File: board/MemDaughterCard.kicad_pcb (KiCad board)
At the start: 2 copper layers, 87 x 67 mm, 13 parts, among them IC1 HM628512LP-7, IC2 HM628512LP-7, IC3 HM628512LP-7, IC4 HM628512LP-7, J1 Conn_01x32, J2 Conn_01x24, J3 E D C B A 9 8 7 6 5 4 3 2 1 0, U1 74HC139

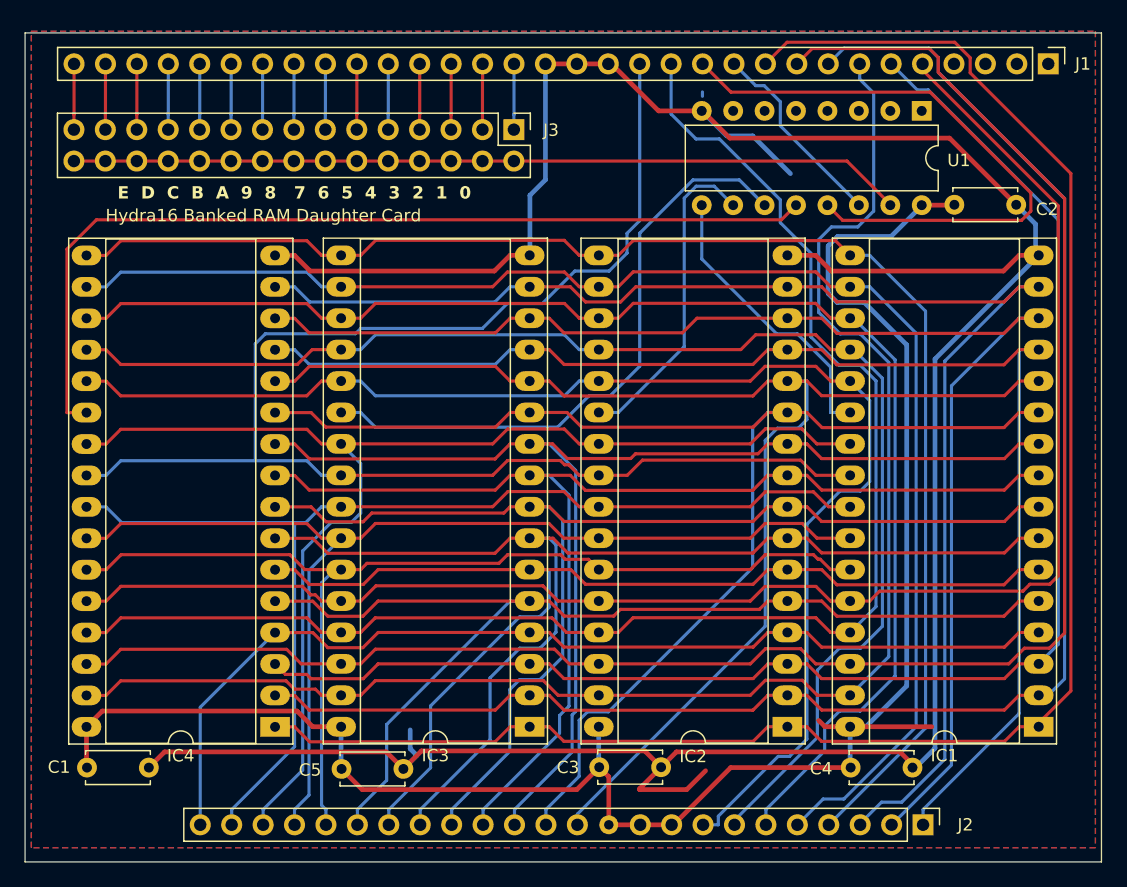
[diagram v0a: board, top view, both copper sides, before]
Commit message: Added surface mount version of memory daughter cards, and lots of schematic updates and fixes, including adding dedicated registers for shared memory bank select at $FFF1 and IRQ vTable entry selector at $FFF2 along with the IRQ vTable registers and priority encoders for 16 IRQs
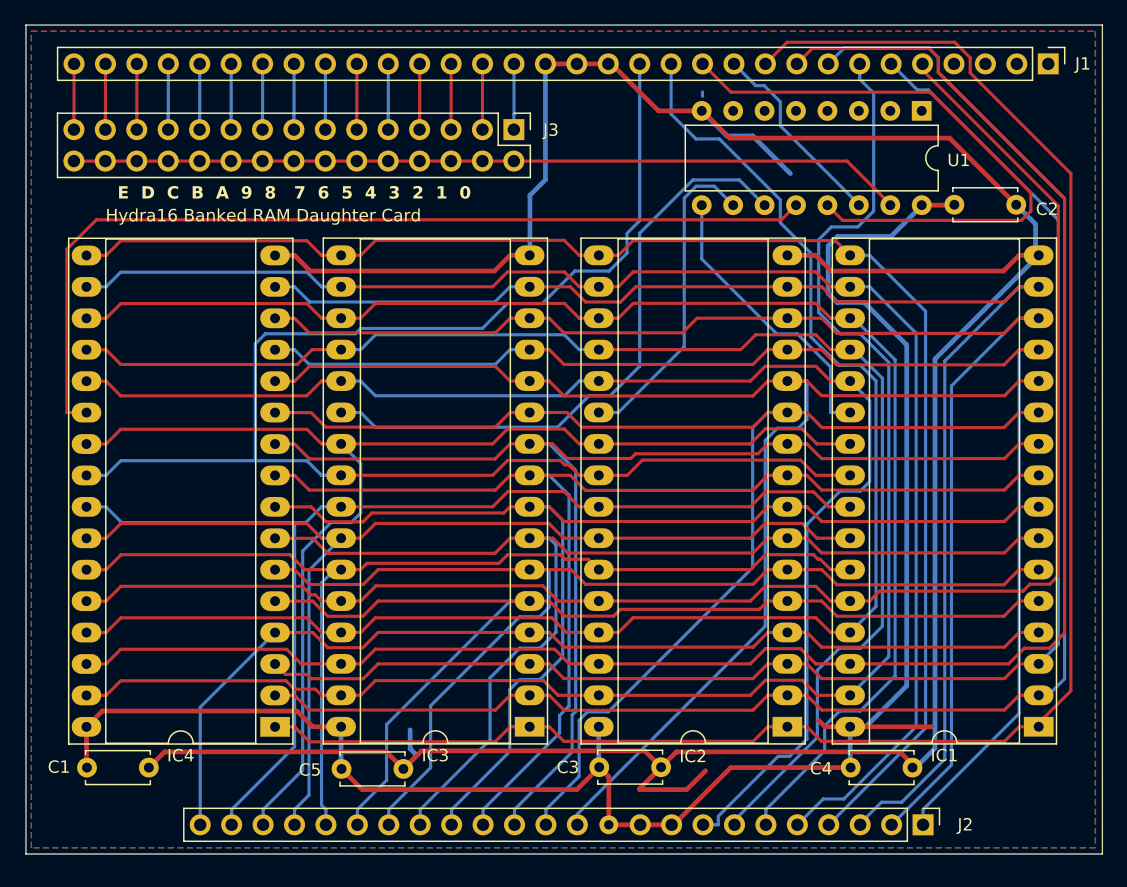
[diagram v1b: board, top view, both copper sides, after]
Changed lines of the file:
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@@
 	)
 	(gr_rect
-		(start 106.032 68.8939)
-		(end 193.032 135.8939)
+		(start 106.106 68.255)
+		(end 193.106 135.255)
 		(stroke
 			(width 0.05)
